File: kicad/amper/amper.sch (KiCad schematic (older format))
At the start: 53 parts, among them J1 Conn_02x05_Odd_Even, J2 Conn_02x05_Odd_Even, J3 USB_C_Receptacle_USB2.0, J4 Conn_01x05, J5 Conn_02x05_Odd_Even, J6 Conn_01x03, J7 Conn_01x04, Q1 FDS9435A, Q2 FDS9435A, SW1 SW_Push, SW2 SW_Push, SW3 SW_Push, SW4 SW_Push, U1 114-87-308-41-134161, U2 HDSM-441B, U3 HDSM-441B, U4 HDSM-441B, U5 TM1637, U6 ATtiny1606-S, U7 UA741CP

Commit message: Reannotated everything
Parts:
- renumbered C9 to C10, C10 to C11, C11 to C5, C5 to C6, C6 to C7, C7 to C8, C8 to C9, J5 to J3, J3 to J4, J6 to J5, J7 to J6, J4 to J7, U5 to U1, U1 to U5, U7 to U6, U6 to U7

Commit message: most of the large components in place, started laying tracks
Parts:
- J4: footprint (none) -> amper:MC-303S
- U6: footprint amper:MC-303S -> (none)
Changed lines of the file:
@@
 F 0 "U6" H 6050 7250 50  0000 L CNN
 F 1 "UA741CP" H 6100 7150 50  0000 L CNN
-F 2 "amper:MC-303S" H 6100 7050 50  0001 C CNN
+F 2 "" H 6100 7050 50  0001 C CNN
 F 3 "~" H 6200 7150 50  0001 C CNN
 F 4 "LCSC" H 6050 7000 50  0001 C CNN "Vendor"
@@
 F 0 "J4" H 9157 5067 50  0000 C CNN
 F 1 "USB_C_Receptacle_USB2.0" H 9157 4976 50  0000 C CNN
-F 2 "" H 9200 4200 50  0001 C CNN
+F 2 "amper:MC-303S" H 9200 4200 50  0001 C CNN
 F 3 "https://www.usb.org/sites/default/files/documents/usb_type-c.zip" H 9200 4200 50  0001 C CNN
 	1    9050 4200

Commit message: Layed out symetrical 7 seg and driver circuits
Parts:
- U5: footprint amper:114-87-308-41-134161 -> amper:114-87-308-41-134161-generated
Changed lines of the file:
@@
 F 0 "U5" H 4600 7250 50  0000 L CNN
 F 1 "114-87-308-41-134161" H 4650 7150 50  0000 L CNN
-F 2 "amper:114-87-308-41-134161" H 4650 7050 50  0001 C CNN
+F 2 "amper:114-87-308-41-134161-generated" H 4650 7050 50  0001 C CNN
 F 3 "~" H 4750 7150 50  0001 C CNN
 F 4 "Not LCSC" H 4600 7000 50  0001 C CNN "Vendor"

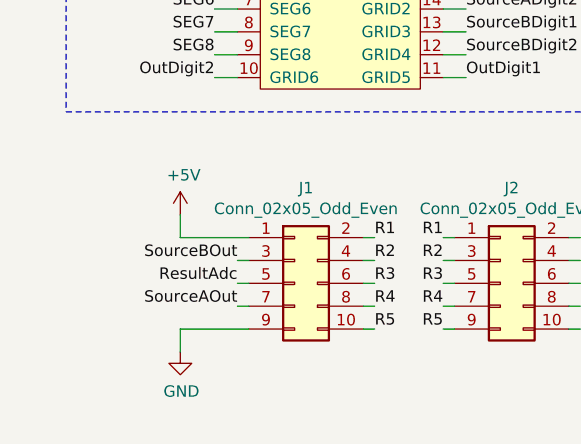
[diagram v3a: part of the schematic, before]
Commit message: added symbols, Routed very centre of board
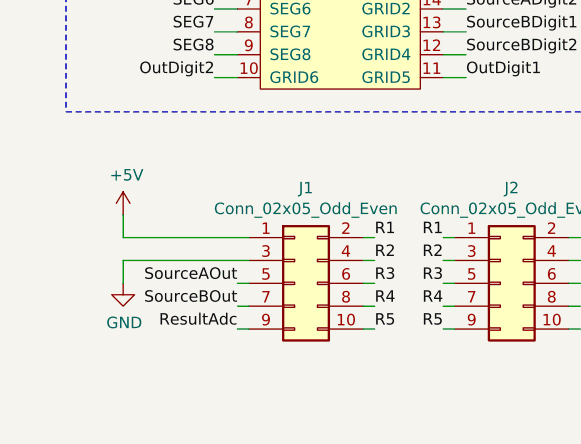
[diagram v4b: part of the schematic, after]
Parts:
- J1: footprint amper:2.54_2x5_alternate -> amper:2.54_2x5_alternate-source-side
- J3: footprint amper:2.54_2x5_alternate -> amper:2.54_2x5_alternate-opamp-side
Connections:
- net GND: now also J1.3 (Pin_3); no longer J1.9 (Pin_9)
- net ResultAdc: now also J1.9 (Pin_9); no longer J1.5 (Pin_5)
- net SourceAOut: now also J1.5 (Pin_5); no longer J1.7 (Pin_7)
- net SourceBOut: now also J1.7 (Pin_7); no longer J1.3 (Pin_3)
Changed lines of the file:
@@
 F 0 "J3" H 3550 7417 50  0000 C CNN
 F 1 "Conn_02x05_Odd_Even" H 3550 7326 50  0000 C CNN
-F 2 "amper:2.54_2x5_alternate" H 3500 7000 50  0001 C CNN
+F 2 "amper:2.54_2x5_alternate-opamp-side" H 3500 7000 50  0001 C CNN
 F 3 "~" H 3500 7000 50  0001 C CNN
 	1    3500 7000
@@
 F 0 "J1" H 1750 7417 50  0000 C CNN
 F 1 "Conn_02x05_Odd_Even" H 1750 7326 50  0000 C CNN
-F 2 "amper:2.54_2x5_alternate" H 1700 7000 50  0001 C CNN
+F 2 "amper:2.54_2x5_alternate-source-side" H 1700 7000 50  0001 C CNN
 F 3 "~" H 1700 7000 50  0001 C CNN
 	1    1700 7000
 	1    0    0    -1
 $EndComp
-Text Label 1450 6900 2    50   ~ 0
+Text Label 1450 7100 2    50   ~ 0
 SourceBOut
-Text Label 1450 7000 2    50   ~ 0
+Text Label 1450 7200 2    50   ~ 0
 ResultAdc
-Text Label 1450 7100 2    50   ~ 0
-SourceAOut
+Wire Wire Line
+	1450 7200 1500 7200
 Wire Wire Line
 	1500 7100 1450 7100
-Wire Wire Line
-	1450 7000 1500 7000
-Wire Wire Line
-	1500 6900 1450 6900
 Text Label 2050 6800 0    50   ~ 0
 R1
@@
 L power:+5V #PWR04
 U 1 1 62C63EF1
-P 1200 6700
-F 0 "#PWR04" H 1200 6550 50  0001 C CNN
-F 1 "+5V" H 1215 6873 50  0000 C CNN
-F 2 "" H 1200 6700 50  0001 C CNN
-F 3 "" H 1200 6700 50  0001 C CNN
-	1    1200 6700
+P 950 6700
+F 0 "#PWR04" H 950 6550 50  0001 C CNN
+F 1 "+5V" H 965 6873 50  0000 C CNN
+F 2 "" H 950 6700 50  0001 C CNN
+F 3 "" H 950 6700 50  0001 C CNN
+	1    950  6700
 	1    0    0    -1
 $EndComp
 Wire Wire Line
-	1200 6700 1200 6800
-Wire Wire Line
-	1200 6800 1500 6800
+	950  6700 950  6800
 $Comp
 L power:GND #PWR05
 U 1 1 62C77E5E
-P 1200 7300
-F 0 "#PWR05" H 1200 7050 50  0001 C CNN
-F 1 "GND" H 1205 7127 50  0000 C CNN
-F 2 "" H 1200 7300 50  0001 C CNN
-F 3 "" H 1200 7300 50  0001 C CNN
-	1    1200 7300
+P 950 7000
+F 0 "#PWR05" H 950 6750 50  0001 C CNN
+F 1 "GND" H 955 6827 50  0000 C CNN
+F 2 "" H 950 7000 50  0001 C CNN
+F 3 "" H 950 7000 50  0001 C CNN
+	1    950  7000
 	1    0    0    -1
 $EndComp
 Wire Wire Line
-	1200 7300 1200 7200
+	950  7000 950  6900
 Wire Wire Line
-	1200 7200 1500 7200
+	1500 7000 1450 7000
+Text Label 1450 7000 2    50   ~ 0
+SourceAOut
+Wire Wire Line
+	950  6900 1500 6900
+Wire Wire Line
+	950  6800 1500 6800
 $EndSCHEMATC

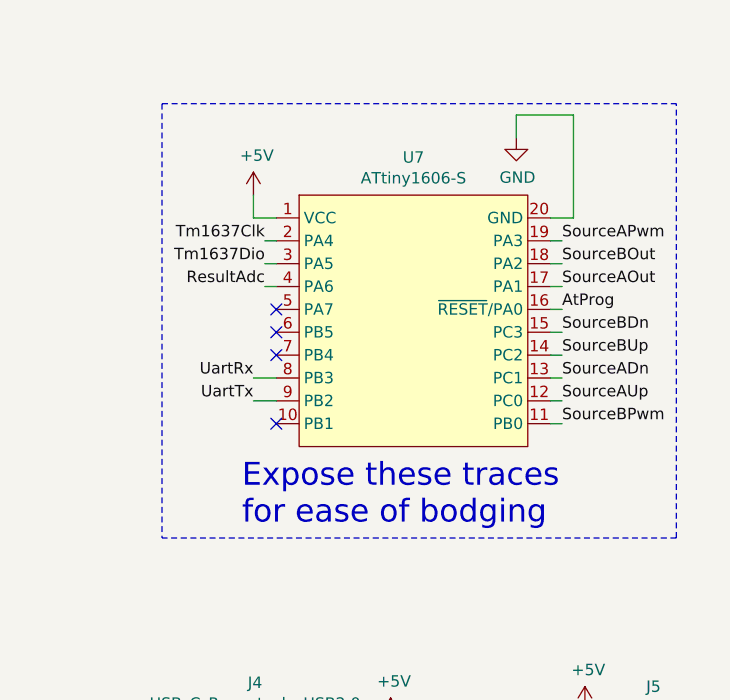
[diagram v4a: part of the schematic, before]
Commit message: New layout with boxes
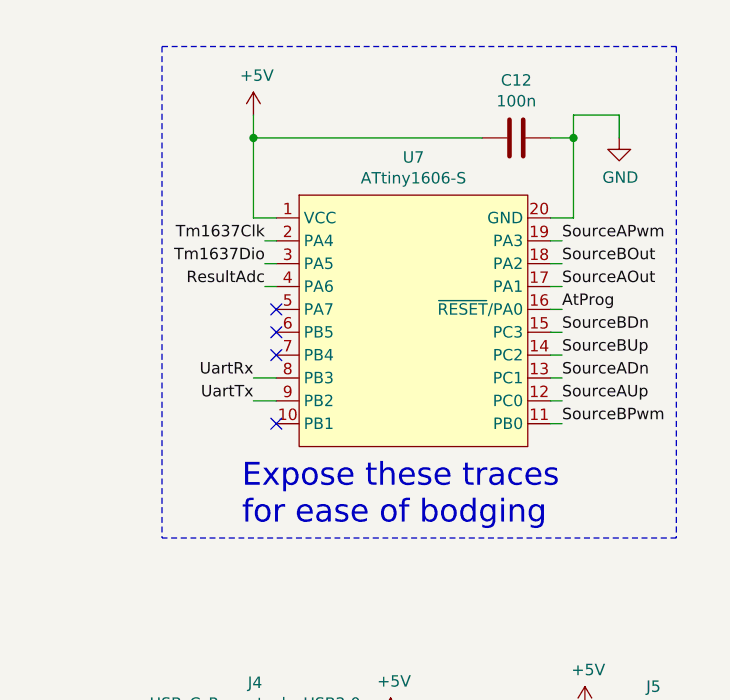
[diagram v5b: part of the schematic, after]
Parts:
- added C12: 100n, Capacitor_SMD:C_0603_1608Metric_Pad1.05x0.95mm_HandSolder, symbol Device:C
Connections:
- net +5V: now also C12.2
- net GND: now also C12.1
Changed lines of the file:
@@
 L power:+5V #PWR017
 U 1 1 622DD6E8
-P 9150 1200
-F 0 "#PWR017" H 9150 1050 50  0001 C CNN
-F 1 "+5V" H 9165 1373 50  0000 C CNN
-F 2 "" H 9150 1200 50  0001 C CNN
-F 3 "" H 9150 1200 50  0001 C CNN
-	1    9150 1200
-	1    0    0    -1
-$EndComp
-Wire Wire Line
-	9150 1200 9150 1300
+P 9150 850
+F 0 "#PWR017" H 9150 700 50  0001 C CNN
+F 1 "+5V" H 9165 1023 50  0000 C CNN
+F 2 "" H 9150 850 50  0001 C CNN
+F 3 "" H 9150 850 50  0001 C CNN
+	1    9150 850
+	1    0    0    -1
+$EndComp
 Wire Wire Line
 	9150 1300 9250 1300
@@
 L power:GND #PWR022
 U 1 1 622EC3F9
-P 10300 950
-F 0 "#PWR022" H 10300 700 50  0001 C CNN
-F 1 "GND" H 10305 777 50  0000 C CNN
-F 2 "" H 10300 950 50  0001 C CNN
-F 3 "" H 10300 950 50  0001 C CNN
-	1    10300 950
-	1    0    0    -1
-$EndComp
-Wire Wire Line
-	10550 1300 10550 850
-Wire Wire Line
-	10550 850  10300 850
-Wire Wire Line
-	10300 850  10300 950
+P 10750 950
+F 0 "#PWR022" H 10750 700 50  0001 C CNN
+F 1 "GND" H 10755 777 50  0000 C CNN
+F 2 "" H 10750 950 50  0001 C CNN
+F 3 "" H 10750 950 50  0001 C CNN
+	1    10750 950
+	1    0    0    -1
+$EndComp
+Wire Wire Line
+	10550 1300 10550 950
+Wire Wire Line
+	10750 850  10750 950
 Text Label 10500 1700 0    50   ~ 0
 AtProg
@@
 	11000 2700 8750 2700
 Wire Notes Line
-	8750 800  11000 800
-Wire Notes Line
-	8750 800  8750 2700
-Wire Notes Line
-	11000 2700 11000 800
+	8750 550  11000 550
 $Comp
 L Connector_Generic:Conn_01x05 J7
@@
 Wire Wire Line
 	950  6800 1500 6800
+$Comp
+L Device:C C12
+U 1 1 62E8013E
+P 10300 950
+F 0 "C12" V 10048 950 50  0000 C CNN
+F 1 "100n" V 10139 950 50  0000 C CNN
+F 2 "Capacitor_SMD:C_0603_1608Metric_Pad1.05x0.95mm_HandSolder" H 10338 800 50  0001 C CNN
+F 3 "~" H 10300 950 50  0001 C CNN
+	1    10300 950
+	0    1    1    0
+$EndComp
+Wire Wire Line
+	10550 850  10750 850
+Wire Wire Line
+	10450 950  10550 950
+Connection ~ 10550 950
+Wire Wire Line
+	10550 950  10550 850
+Wire Wire Line
+	10150 950  9150 950
+Wire Wire Line
+	9150 950  9150 1300
+Wire Wire Line
+	9150 950  9150 850
+Connection ~ 9150 950
+Wire Notes Line
+	8750 550  8750 2700
+Wire Notes Line
+	11000 550  11000 2700
 $EndSCHEMATC

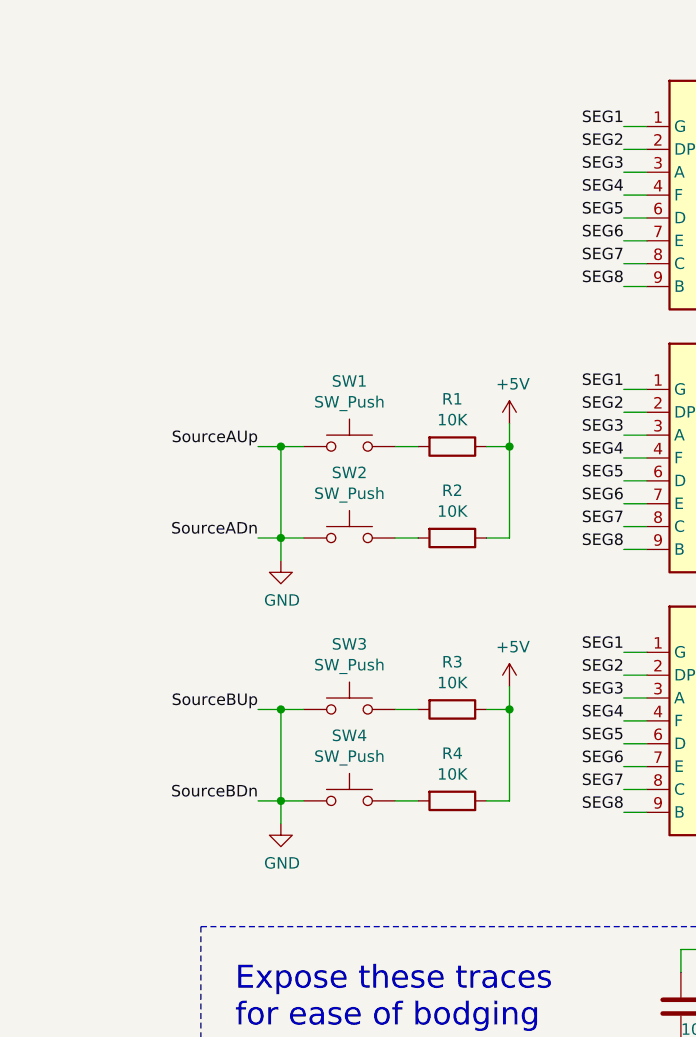
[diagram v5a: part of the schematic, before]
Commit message: Added USB socket and boxes with A, B and output symbols. Local routing started
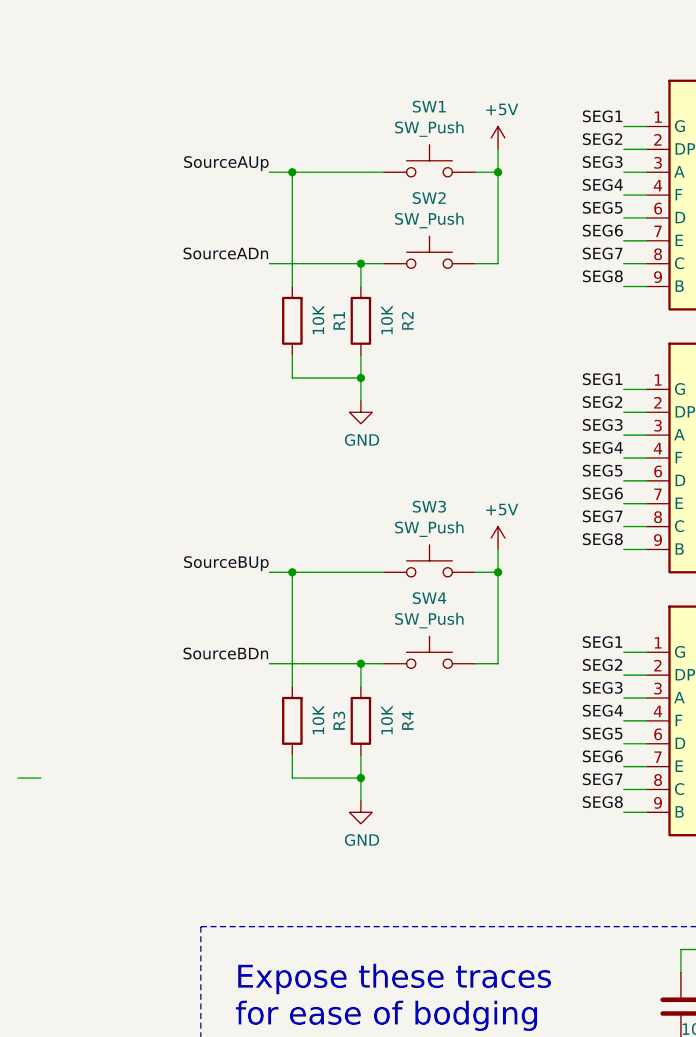
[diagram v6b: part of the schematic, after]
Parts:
- SW1, SW3: footprint amper:K2-1157SP-I4SW-01 -> amper:UpSwitch
- SW2, SW4: footprint amper:K2-1157SP-I4SW-01 -> amper:DnSwitch
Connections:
- net +5V: now also SW1.2, SW2.2, SW3.2, SW4.2; no longer R1.1, R2.1, R3.1, R4.1
- net GND: now also R1.1, R2.1, R3.1, R4.1; no longer SW1.1, SW2.1, SW3.1, SW4.1, U7.12 (PC0), U7.13 (PC1), U7.14 (PC2), U7.15 (PC3)
- net SourceBUp: now reaches R3.2
- net SourceBUp: now also SW3.1, U7.14 (PC2); no longer SW3.2
- net SourceBDn: now reaches R4.2
- net SourceBDn: now also SW4.1, U7.15 (PC3); no longer SW4.2
- net SourceAUp: now reaches R1.2
- net SourceAUp: now also SW1.1, U7.12 (PC0); no longer SW1.2
- net SourceADn: now reaches R2.2
- net SourceADn: now also SW2.1, U7.13 (PC1); no longer SW2.2
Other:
- moved on the sheet: R1, R2, R3, R4, SW1, SW2, SW3, SW4

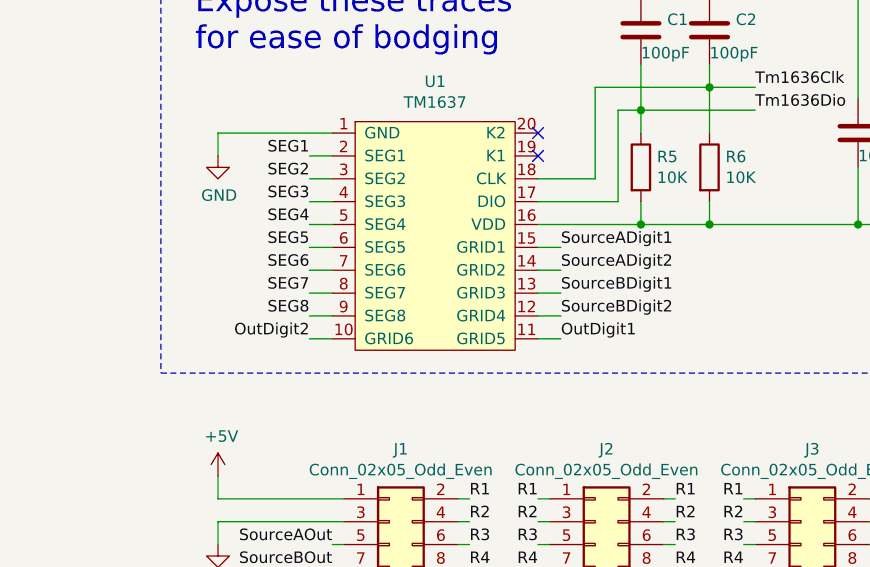
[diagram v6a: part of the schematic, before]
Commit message: Added grid routing
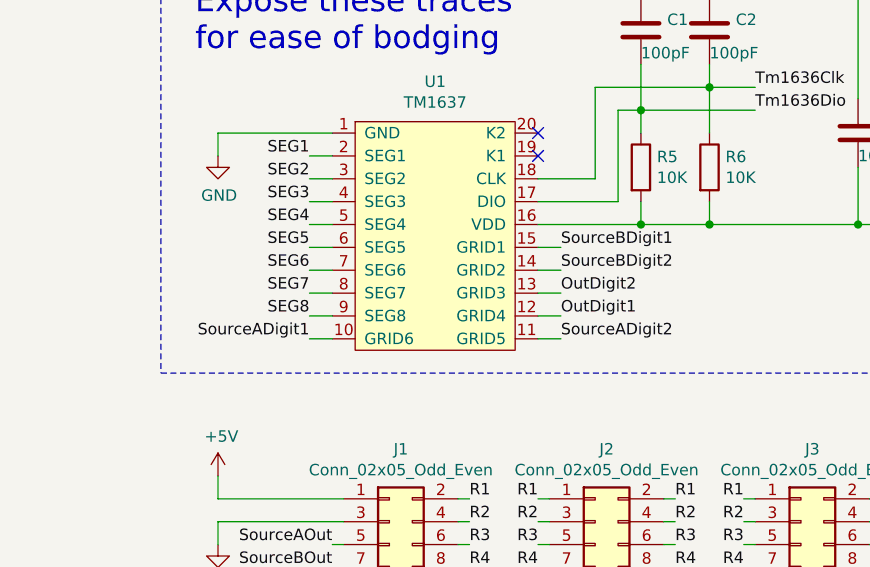
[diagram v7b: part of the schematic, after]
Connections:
- net OutDigit1: now also U1.12 (GRID4); no longer U1.11 (GRID5)
- net OutDigit2: now also U1.13 (GRID3); no longer U1.10 (GRID6)
- net SourceADigit1: now also U1.10 (GRID6); no longer U1.15 (GRID1)
- net SourceADigit2: now also U1.11 (GRID5); no longer U1.14 (GRID2)
- net SourceBDigit1: now also U1.15 (GRID1); no longer U1.13 (GRID3)
- net SourceBDigit2: now also U1.14 (GRID2); no longer U1.12 (GRID4)
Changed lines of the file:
@@
 Wire Wire Line
 	950  5200 1450 5200
+Text Label 1350 6100 2    50   ~ 0
+SourceADigit1
+Text Label 2450 6100 0    50   ~ 0
+SourceADigit2
+Wire Wire Line
+	2350 5700 2450 5700
+Wire Wire Line
+	2350 5800 2450 5800
 Text Label 2450 5700 0    50   ~ 0
-SourceADigit1
+SourceBDigit1
 Text Label 2450 5800 0    50   ~ 0
-SourceADigit2
-Wire Wire Line
-	2350 5700 2450 5700
-Wire Wire Line
-	2350 5800 2450 5800
+SourceBDigit2
+Wire Wire Line
+	2350 5900 2450 5900
+Wire Wire Line
+	2350 6000 2450 6000
+Text Label 2450 6000 0    50   ~ 0
+OutDigit1
 Text Label 2450 5900 0    50   ~ 0
-SourceBDigit1
-Text Label 2450 6000 0    50   ~ 0
-SourceBDigit2
-Wire Wire Line
-	2350 5900 2450 5900
-Wire Wire Line
-	2350 6000 2450 6000
-Text Label 2450 6100 0    50   ~ 0
-OutDigit1
-Text Label 1350 6100 2    50   ~ 0
 OutDigit2
 Wire Wire Line
@@
 	1400 3750 1400 3650
 $Comp
-L power:GND #PWR?
+L power:GND #PWR0101
 U 1 1 6314BDA0
 P 1400 3850
-F 0 "#PWR?" H 1400 3600 50  0001 C CNN
+F 0 "#PWR0101" H 1400 3600 50  0001 C CNN
 F 1 "GND" H 1405 3677 50  0000 C CNN
 F 2 "" H 1400 3850 50  0001 C CNN
@@
 	1900 1500 2000 1500
 $Comp
-L power:+5V #PWR?
+L power:+5V #PWR0102
 U 1 1 631E51F2
 P 2000 1000
-F 0 "#PWR?" H 2000 850 50  0001 C CNN
+F 0 "#PWR0102" H 2000 850 50  0001 C CNN
 F 1 "+5V" H 2015 1173 50  0000 C CNN
 F 2 "" H 2000 1000 50  0001 C CNN
@@
 Connection ~ 1400 2000
 $Comp
-L power:GND #PWR?
+L power:GND #PWR0103
 U 1 1 6328B5C3
 P 1400 2100
-F 0 "#PWR?" H 1400 1850 50  0001 C CNN
+F 0 "#PWR0103" H 1400 1850 50  0001 C CNN
 F 1 "GND" H 1405 1927 50  0000 C CNN
 F 2 "" H 1400 2100 50  0001 C CNN

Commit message: Electrically connected, still needs some work
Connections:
- net Tm1636Clk is gone; now on net Tm1637Clk: C2.2, R6.1, U1.18 (CLK)
- net Tm1636Dio is gone; now on net Tm1637Dio: C1.2, R5.1, U1.17 (DIO)
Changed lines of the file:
@@
 	3100 4500 2800 4500
 Text Label 3300 5100 0    50   ~ 0
-Tm1636Dio
+Tm1637Dio
 Text Label 3300 5000 0    50   ~ 0
-Tm1636Clk
+Tm1637Clk
 $Comp
 L Device:C C3
